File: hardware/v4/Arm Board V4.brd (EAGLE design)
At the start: 108 x 50.8 mm, 28 parts, among them P1 STELLARIS-LAUNCHPADSTELLARIS-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, U1 SN74LS241DW, U2 XBEE-1B3

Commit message: okay i think im done reworking arm board
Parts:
- removed D1: RED, SparkFun-LED:LED-0603
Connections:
- removed net DDATA_OUT: D1.A, U1.2, U1.3
- net DDATA_1: now also U1.2, U1.3; no longer D1.C
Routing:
- net DDATA_1: track 19.6 -> 107.1 mm, vias 0 -> 2
- net DDATA_OUT: track 87.2 -> 0.00 mm, vias 2 -> 0
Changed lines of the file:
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@@
 <layer number="18" name="Vias" color="2" fill="1" visible="yes" active="yes"/>
 <layer number="19" name="Unrouted" color="6" fill="1" visible="yes" active="yes"/>
-<layer number="20" name="Dimension" color="15" fill="1" visible="yes" active="yes"/>
+<layer number="20" name="Dimension" color="15" fill="1" visible="no" active="yes"/>
 <layer number="21" name="tPlace" color="7" fill="1" visible="yes" active="yes"/>
 <layer number="22" name="bPlace" color="7" fill="1" visible="yes" active="yes"/>
-<layer number="23" name="tOrigins" color="15" fill="1" visible="yes" active="yes"/>
-<layer number="24" name="bOrigins" color="15" fill="1" visible="yes" active="yes"/>
+<layer number="23" name="tOrigins" color="15" fill="1" visible="no" active="yes"/>
+<layer number="24" name="bOrigins" color="15" fill="1" visible="no" active="yes"/>
 <layer number="25" name="tNames" color="7" fill="1" visible="yes" active="yes"/>
 <layer number="26" name="bNames" color="7" fill="1" visible="yes" active="yes"/>
@@
 </element>
 <element name="U$1" library="MRDT-RoboticArm" package="TORXIS_BREAKOUT" value="TORXIS_BREAKOUT" x="107.95" y="0" rot="R90"/>
-<element name="D1" library="SparkFun-LED" package="LED-0603" value="RED" x="75.438" y="41.148" rot="R270">
-<attribute name="PROD_ID" value="DIO-00819" x="75.438" y="41.148" size="1.778" layer="27" rot="R270" display="off"/>
-</element>
 </elements>
 <signals>
@@
 <wire x1="48.006" y1="16" x2="47.5" y2="16" width="0.4064" layer="1"/>
 <wire x1="47.5" y1="16" x2="47.498" y2="16.002" width="0.4064" layer="1"/>
-<wire x1="51.193" y1="30.849" x2="51.816" y2="30.226" width="0.4064" layer="1"/>
 <wire x1="51.816" y1="30.226" x2="51.816" y2="21.336" width="0.4064" layer="1"/>
 <wire x1="51.816" y1="21.336" x2="51.054" y2="20.574" width="0.4064" layer="1"/>
@@
 <wire x1="50.038" y1="31.0395" x2="50.2285" y2="30.722" width="0.4064" layer="16"/>
 <via x="50.2285" y="30.722" extent="1-16" drill="0.5"/>
-<wire x1="50.2285" y1="30.722" x2="51.193" y2="30.849" width="0.4064" layer="1"/>
 <wire x1="50.038" y1="32.766" x2="50.038" y2="33.528" width="0.4064" layer="1"/>
 <wire x1="50.038" y1="33.528" x2="49.53" y2="34.036" width="0.4064" layer="1"/>
 <wire x1="49.53" y1="34.036" x2="34.29" y2="34.036" width="0.4064" layer="1"/>
 <wire x1="34.29" y1="34.036" x2="33.274" y2="35.052" width="0.4064" layer="1"/>
+<wire x1="51.816" y1="30.226" x2="51.308" y2="30.734" width="0.4064" layer="1"/>
+<wire x1="51.308" y1="30.734" x2="50.2405" y2="30.734" width="0.4064" layer="1"/>
+<wire x1="50.2405" y1="30.734" x2="50.2285" y2="30.722" width="0.4064" layer="1"/>
 </signal>
 <signal name="RX_1">
@@
 <contactref element="JP9" pad="3"/>
 <wire x1="84.29625" y1="41.11625" x2="78.58125" y2="41.11625" width="0.4064" layer="1"/>
-<contactref element="D1" pad="C"/>
-<wire x1="78.486" y1="41.11625" x2="76.21975" y2="41.11625" width="0.4064" layer="1"/>
-<wire x1="76.21975" y1="41.11625" x2="76.188" y2="41.148" width="0.4064" layer="1"/>
-<wire x1="78.58125" y1="41.11625" x2="78.486" y2="41.11625" width="0.4064" layer="1"/>
+<contactref element="U1" pad="2"/>
+<contactref element="U1" pad="3"/>
+<wire x1="16.38935" y1="14.85265" x2="16.51" y2="14.732" width="0.4064" layer="1"/>
+<wire x1="16.51" y1="14.732" x2="16.51" y2="12.954" width="0.4064" layer="1"/>
+<wire x1="16.51" y1="12.954" x2="17.272" y2="12.192" width="0.4064" layer="1"/>
+<wire x1="17.272" y1="12.192" x2="32.004" y2="12.192" width="0.4064" layer="1"/>
+<wire x1="32.004" y1="12.192" x2="33.02" y2="13.208" width="0.4064" layer="1"/>
+<wire x1="33.02" y1="13.208" x2="33.02" y2="22.606" width="0.4064" layer="1"/>
+<wire x1="33.02" y1="22.606" x2="34.544" y2="24.13" width="0.4064" layer="1"/>
+<wire x1="34.544" y1="24.13" x2="43.18" y2="24.13" width="0.4064" layer="1"/>
+<via x="43.18" y="24.13" extent="1-16" drill="0.5"/>
+<wire x1="43.18" y1="24.13" x2="53.594" y2="24.13" width="0.4064" layer="16"/>
+<via x="53.594" y="24.13" extent="1-16" drill="0.5"/>
+<wire x1="53.594" y1="24.13" x2="71.374" y2="24.13" width="0.4064" layer="1"/>
+<wire x1="71.374" y1="24.13" x2="72.39" y2="25.146" width="0.4064" layer="1"/>
+<wire x1="72.39" y1="25.146" x2="72.39" y2="38.862" width="0.4064" layer="1"/>
+<wire x1="16.38935" y1="14.85265" x2="16.51" y2="14.85265" width="0.4064" layer="1"/>
+<wire x1="72.39" y1="38.862" x2="74.676" y2="41.148" width="0.4064" layer="1"/>
+<wire x1="15.24" y1="14.85265" x2="16.38935" y2="14.85265" width="0" layer="19" extent="1-1"/>
+<wire x1="74.676" y1="41.148" x2="78.5495" y2="41.148" width="0.4064" layer="1"/>
+<wire x1="78.5495" y1="41.148" x2="78.58125" y2="41.11625" width="0.4064" layer="1"/>
 </signal>
 <signal name="N$7">
@@
 <contactref element="U$1" pad="B"/>
 </signal>
-<signal name="DDATA_OUT">
-<contactref element="U1" pad="3"/>
-<contactref element="D1" pad="A"/>
-<contactref element="U1" pad="2"/>
-<wire x1="15.24" y1="14.85265" x2="16.38935" y2="14.85265" width="0.4064" layer="1"/>
-<wire x1="16.38935" y1="14.85265" x2="16.51" y2="14.732" width="0.4064" layer="1"/>
-<wire x1="16.51" y1="14.732" x2="16.51" y2="12.954" width="0.4064" layer="1"/>
-<wire x1="16.51" y1="12.954" x2="17.272" y2="12.192" width="0.4064" layer="1"/>
-<wire x1="17.272" y1="12.192" x2="32.004" y2="12.192" width="0.4064" layer="1"/>
-<wire x1="32.004" y1="12.192" x2="33.02" y2="13.208" width="0.4064" layer="1"/>
-<wire x1="33.02" y1="13.208" x2="33.02" y2="22.606" width="0.4064" layer="1"/>
-<wire x1="33.02" y1="22.606" x2="34.544" y2="24.13" width="0.4064" layer="1"/>
-<wire x1="34.544" y1="24.13" x2="43.18" y2="24.13" width="0.4064" layer="1"/>
-<via x="43.18" y="24.13" extent="1-16" drill="0.5"/>
-<wire x1="43.18" y1="24.13" x2="53.594" y2="24.13" width="0.4064" layer="16"/>
-<via x="53.594" y="24.13" extent="1-16" drill="0.5"/>
-<wire x1="53.594" y1="24.13" x2="71.374" y2="24.13" width="0.4064" layer="1"/>
-<wire x1="71.374" y1="24.13" x2="72.39" y2="25.146" width="0.4064" layer="1"/>
-<wire x1="72.39" y1="25.146" x2="72.39" y2="38.862" width="0.4064" layer="1"/>
-<wire x1="72.39" y1="38.862" x2="74.676" y2="41.148" width="0.4064" layer="1"/>
-<wire x1="74.688" y1="41.148" x2="74.676" y2="41.148" width="0.4064" layer="1"/>
-<wire x1="16.38935" y1="14.85265" x2="16.51" y2="14.85265" width="0.4064" layer="1"/>
-</signal>
 <signal name="N$10">

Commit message: okay now im done
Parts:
- added D1: RED, SparkFun-LED:LED-0603
- added R1: 1k, SparkFun-Resistors:1206
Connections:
- new net N$13: D1.A, R1.1
- net +5V: now also R1.2, U$1.+5V_OUT
- net DDATA_1: now also D1.C
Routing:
- net DDATA_1: track 107.1 -> 113.5 mm
- net N$13: track 0.00 -> 3.93 mm
- net +5V: track 186.8 -> 189.1 mm
- removed copper zone on layer 16, net N$10
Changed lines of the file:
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@@
 <layer number="17" name="Pads" color="2" fill="1" visible="yes" active="yes"/>
 <layer number="18" name="Vias" color="2" fill="1" visible="yes" active="yes"/>
-<layer number="19" name="Unrouted" color="6" fill="1" visible="yes" active="yes"/>
+<layer number="19" name="Unrouted" color="6" fill="1" visible="no" active="yes"/>
 <layer number="20" name="Dimension" color="15" fill="1" visible="no" active="yes"/>
 <layer number="21" name="tPlace" color="7" fill="1" visible="yes" active="yes"/>
 <layer number="22" name="bPlace" color="7" fill="1" visible="yes" active="yes"/>
-<layer number="23" name="tOrigins" color="15" fill="1" visible="no" active="yes"/>
-<layer number="24" name="bOrigins" color="15" fill="1" visible="no" active="yes"/>
+<layer number="23" name="tOrigins" color="15" fill="1" visible="yes" active="yes"/>
+<layer number="24" name="bOrigins" color="15" fill="1" visible="yes" active="yes"/>
 <layer number="25" name="tNames" color="7" fill="1" visible="yes" active="yes"/>
 <layer number="26" name="bNames" color="7" fill="1" visible="yes" active="yes"/>
@@
 <layer number="46" name="Milling" color="3" fill="1" visible="no" active="yes"/>
 <layer number="47" name="Measures" color="7" fill="1" visible="no" active="yes"/>
-<layer number="48" name="Document" color="7" fill="1" visible="yes" active="yes"/>
+<layer number="48" name="Document" color="7" fill="1" visible="no" active="yes"/>
 <layer number="49" name="Reference" color="7" fill="1" visible="yes" active="yes"/>
 <layer number="50" name="dxf" color="7" fill="1" visible="no" active="no"/>
@@
 <text x="50.2285" y="31.75" size="0.6096" layer="21" font="vector" ratio="15" rot="SR180" align="center">DOUT</text>
 <text x="45.7835" y="31.75" size="0.6096" layer="21" font="vector" ratio="15" rot="SR180" align="center">PWR</text>
-<text x="2.667" y="30.226" size="1.016" layer="21" font="vector" rot="R90" align="top-center">Missouri S&amp;T
+<text x="1.905" y="25.654" size="1.016" layer="21" font="vector" rot="R90" align="top-center">Missouri S&amp;T
 Mars Rover Design Team
 Robotic Arm Board
@@
 <text x="66.548" y="41.529" size="0.8128" layer="21" font="vector" rot="SR0" align="center">+ 12VIN -</text>
 <rectangle x1="15.65275" y1="26.67" x2="18.19275" y2="29.21" layer="41"/>
-<text x="91.91625" y="43.65625" size="0.6096" layer="21" font="vector" rot="SR270" align="center">MX</text>
-<text x="97.63125" y="43.65625" size="0.6096" layer="21" font="vector" rot="SR270" align="center">MX</text>
-<text x="86.36" y="43.65625" size="0.6096" layer="21" font="vector" rot="SR270" align="center">MX</text>
-<text x="80.645" y="43.4975" size="0.6096" layer="21" font="vector" rot="SR270" align="center">MX</text>
+<text x="91.97975" y="43.71975" size="0.6096" layer="21" font="vector" rot="SR90" align="center">MX</text>
+<text x="97.44075" y="43.71975" size="0.6096" layer="21" font="vector" rot="SR90" align="center">MX</text>
+<text x="86.106" y="43.71975" size="0.6096" layer="21" font="vector" rot="SR90" align="center">MX</text>
+<text x="80.391" y="43.8785" size="0.6096" layer="21" font="vector" rot="SR90" align="center">MX</text>
 <text x="76.99375" y="43.65625" size="0.6096" layer="21" font="vector" rot="R270" align="top-center">DAT  12V  GND</text>
 <wire x1="0" y1="0" x2="0" y2="50.8" width="0" layer="20"/>
@@
 </element>
 <element name="U$1" library="MRDT-RoboticArm" package="TORXIS_BREAKOUT" value="TORXIS_BREAKOUT" x="107.95" y="0" rot="R90"/>
+<element name="R1" library="SparkFun-Resistors" package="1206" value="1k" x="82.55" y="36.703" rot="R270"/>
+<element name="D1" library="SparkFun-LED" package="LED-0603" value="RED" x="78.74" y="37.084" rot="R90">
+<attribute name="PROD_ID" value="DIO-00819" x="78.74" y="37.084" size="1.778" layer="27" rot="R90" display="off"/>
+</element>
 </elements>
 <signals>
@@
 <wire x1="33.528" y1="45.466" x2="33.528" y2="46.482" width="0.4064" layer="1"/>
 <wire x1="33.528" y1="46.482" x2="33.02" y2="46.99" width="0.4064" layer="1"/>
-<wire x1="37.6555" y1="41.656" x2="37.084" y2="41.656" width="0.4064" layer="1"/>
-<wire x1="37.084" y1="41.656" x2="36.576" y2="41.148" width="0.4064" layer="1"/>
-<wire x1="36.576" y1="41.148" x2="36.576" y2="38.735" width="0.4064" layer="1"/>
-<wire x1="36.576" y1="38.735" x2="36.83" y2="38.481" width="0.4064" layer="1"/>
 <wire x1="52.07" y1="40.132" x2="52.705" y2="39.624" width="0.4064" layer="1"/>
 <wire x1="52.705" y1="39.624" x2="52.705" y2="38.735" width="0.4064" layer="1"/>
@@
 <wire x1="49.2125" y1="40.132" x2="47.5615" y2="38.481" width="0.4064" layer="1"/>
 <wire x1="47.5615" y1="38.481" x2="40.64" y2="38.481" width="0.4064" layer="1"/>
-<wire x1="40.64" y1="38.481" x2="36.83" y2="38.481" width="0.4064" layer="1"/>
-<wire x1="34.8615" y1="41.151" x2="36.573" y2="41.151" width="0.4064" layer="1"/>
-<wire x1="36.573" y1="41.151" x2="36.576" y2="41.148" width="0.4064" layer="1"/>
+<wire x1="40.64" y1="38.481" x2="36.957" y2="38.481" width="0.4064" layer="1"/>
 <wire x1="8.89" y1="5.08" x2="8.89" y2="6.604" width="0.8128" layer="16"/>
 <wire x1="8.89" y1="6.604" x2="9.398" y2="7.112" width="0.8128" layer="16"/>
@@
 <wire x1="53.975" y1="34.925" x2="57.404" y2="31.496" width="0.8128" layer="16"/>
 <wire x1="57.404" y1="22.352" x2="57.404" y2="31.496" width="0.8128" layer="16"/>
+<contactref element="R1" pad="2"/>
+<contactref element="U$1" pad="+5V_OUT"/>
+<wire x1="82.55" y1="33.02" x2="82.55" y2="35.303" width="0.4064" layer="1"/>
+<wire x1="36.957" y1="38.481" x2="36.576" y2="38.862" width="0.4064" layer="1"/>
+<wire x1="36.576" y1="38.862" x2="36.576" y2="40.897" width="0.4064" layer="1"/>
+<wire x1="34.8615" y1="41.151" x2="36.322" y2="41.151" width="0.4064" layer="1"/>
+<wire x1="36.322" y1="41.151" x2="36.4505" y2="41.0225" width="0.4064" layer="1"/>
+<wire x1="36.4505" y1="41.0225" x2="36.576" y2="40.897" width="0.4064" layer="1"/>
+<wire x1="37.6555" y1="41.656" x2="37.084" y2="41.656" width="0.4064" layer="1"/>
+<wire x1="37.084" y1="41.656" x2="36.4505" y2="41.0225" width="0.4064" layer="1"/>
+<wire x1="57.404" y1="31.496" x2="82.55" y2="33.02" width="0" layer="19" extent="16-16"/>
 </signal>
 <signal name="+12V">
@@
 <wire x1="16.38935" y1="14.85265" x2="16.51" y2="14.85265" width="0.4064" layer="1"/>
 <wire x1="72.39" y1="38.862" x2="74.676" y2="41.148" width="0.4064" layer="1"/>
-<wire x1="15.24" y1="14.85265" x2="16.38935" y2="14.85265" width="0" layer="19" extent="1-1"/>
-<wire x1="74.676" y1="41.148" x2="78.5495" y2="41.148" width="0.4064" layer="1"/>
+<wire x1="74.676" y1="41.148" x2="75.946" y2="41.148" width="0.4064" layer="1"/>
+<wire x1="75.946" y1="41.148" x2="78.5495" y2="41.148" width="0.4064" layer="1"/>
 <wire x1="78.5495" y1="41.148" x2="78.58125" y2="41.11625" width="0.4064" layer="1"/>
+<contactref element="D1" pad="C"/>
+<wire x1="77.99" y1="37.084" x2="76.2" y2="37.084" width="0.4064" layer="1"/>
+<wire x1="76.2" y1="37.084" x2="75.438" y2="37.846" width="0.4064" layer="1"/>
+<wire x1="75.438" y1="37.846" x2="75.438" y2="40.64" width="0.4064" layer="1"/>
+<wire x1="75.438" y1="40.64" x2="75.946" y2="41.148" width="0.4064" layer="1"/>
+<wire x1="16.38935" y1="14.85265" x2="15.24" y2="14.85265" width="0" layer="19" extent="1-1"/>
 </signal>
 <signal name="N$7">
@@
 <contactref element="U$1" pad="B"/>
 </signal>
-<signal name="N$10">
-<polygon width="0.4064" layer="16">
-<vertex x="100.076" y="12.954"/>
-<vertex x="96.266" y="12.954"/>
-<vertex x="96.266" y="8.89"/>
-<vertex x="96.266" y="4.826"/>
-<vertex x="100.584" y="4.826"/>
-<vertex x="104.394" y="4.826"/>
-<vertex x="104.394" y="9.144"/>
-<vertex x="104.394" y="12.954"/>
-</polygon>
+<signal name="N$13">
+<contactref element="R1" pad="1"/>
+<contactref element="D1" pad="A"/>
+<wire x1="82.55" y1="38.103" x2="82.55" y2="37.338" width="0.4064" layer="1"/>
+<wire x1="82.55" y1="37.338" x2="82.296" y2="37.084" width="0.4064" layer="1"/>
+<wire x1="82.296" y1="37.084" x2="79.49" y2="37.084" width="0.4064" layer="1"/>
 </signal>
 </signals>

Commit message: added refs
added BOM, jrk motor controller ds
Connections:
- net +12V: no longer U$1.VIN
- net GND: no longer U$1.GND@1
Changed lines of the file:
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@@
 <contactref element="JP2" pad="4"/>
 <contactref element="U$1" pad="GND@4"/>
-<contactref element="U$1" pad="GND@1"/>
 <polygon width="0.4064" layer="16" thermals="no">
 <vertex x="0" y="0"/>
@@
 <signal name="+12V">
 <contactref element="U$7" pad="L"/>
-<contactref element="U$1" pad="VIN"/>
 <contactref element="JP9" pad="2"/>
 <contactref element="JP10" pad="2"/>
@@
 <vertex x="61.976" y="50.8"/>
 <vertex x="61.976" y="39.624"/>
-<vertex x="71.374" y="39.624"/>
-<vertex x="74.168" y="42.418"/>
-<vertex x="97.028" y="42.418"/>
-<vertex x="99.568" y="39.878"/>
+<vertex x="71.12" y="39.624"/>
+<vertex x="74.168" y="42.672"/>
+<vertex x="97.028" y="42.672"/>
+<vertex x="99.568" y="40.132"/>
 <vertex x="99.568" y="26.162"/>
 <vertex x="97.028" y="23.622"/>

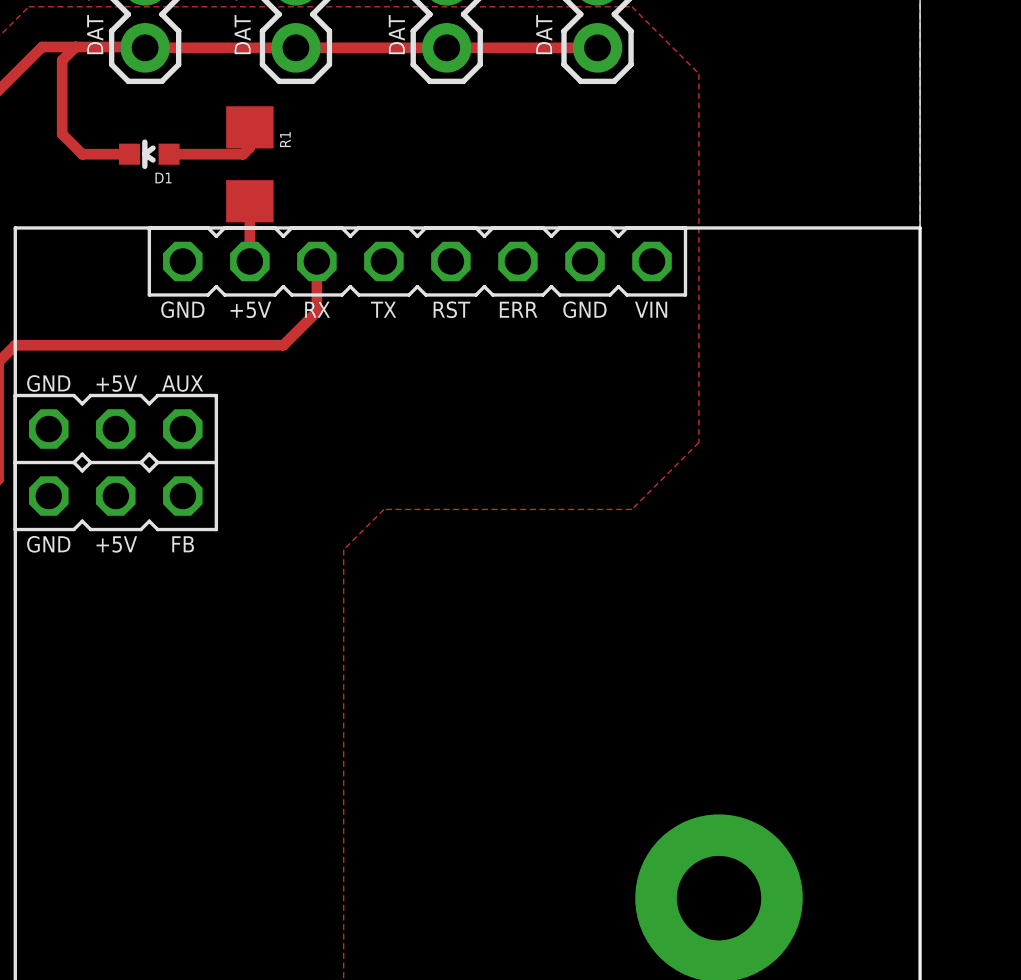
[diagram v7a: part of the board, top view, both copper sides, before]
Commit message: arm board
added parts to allow h-bridge actuator drive
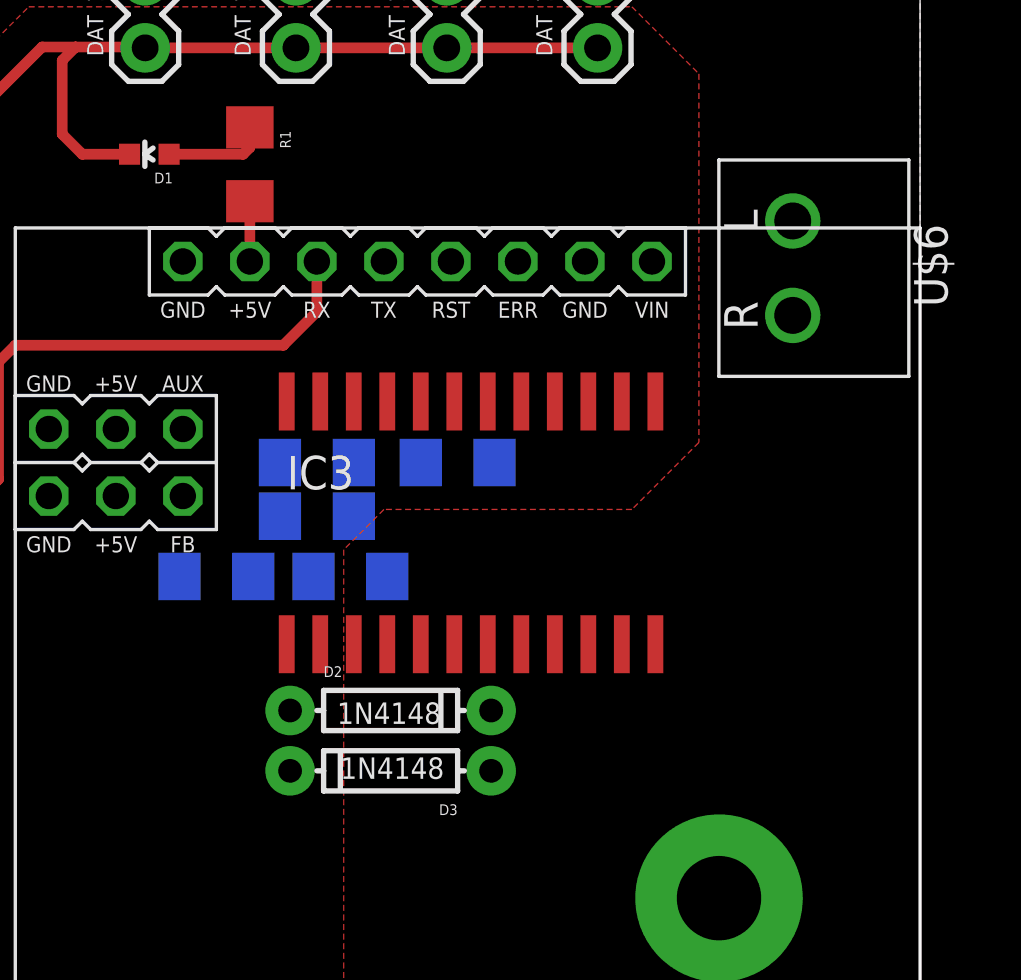
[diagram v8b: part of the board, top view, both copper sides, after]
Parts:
- added C2: 5.6nF, SparkFun-Passives:1206
- added C4: 220nF, SparkFun-Passives:1206
- added C9: 10nF, SparkFun-Passives:1206
- added D2, D3: 1N4148, SparkFun-DiscreteSemi:DIODE-1N4148
- added IC3: L6206D, L6206D:SO24
- added R15: 100, SparkFun-Resistors:1206
- added R8: 100k, SparkFun-Resistors:1206
- added U$6: H_WR-TBL_321*0002VERT, MRDT-2015-PowerBoard:691321100002
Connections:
- new net A1: IC3.5, U$6.L
- new net A2: IC3.21, U$6.R
- new net EN_A: P1.PD2, R8.2
- new net IN1_A: IC3.1, P1.PD3
- new net N$17: D2.C, D3.A, R15.2
- new net N$18: C9.2, R15.1
- new net N$19: C9.1, IC3.22
- new net OCD_A: C2.2, IC3.23, IC3.4, R8.1
- new net VBOOT: C4.2, D3.C, IC3.15
- net +12V: now also C4.1, D2.A, IC3.17, IC3.20
- net GND: now also C2.1, IC3.10, IC3.13, IC3.18, IC3.19, IC3.24, IC3.3, IC3.6, IC3.7
- net IN2_A: now also IC3.2
